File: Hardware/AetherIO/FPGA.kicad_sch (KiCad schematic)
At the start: 3 parts

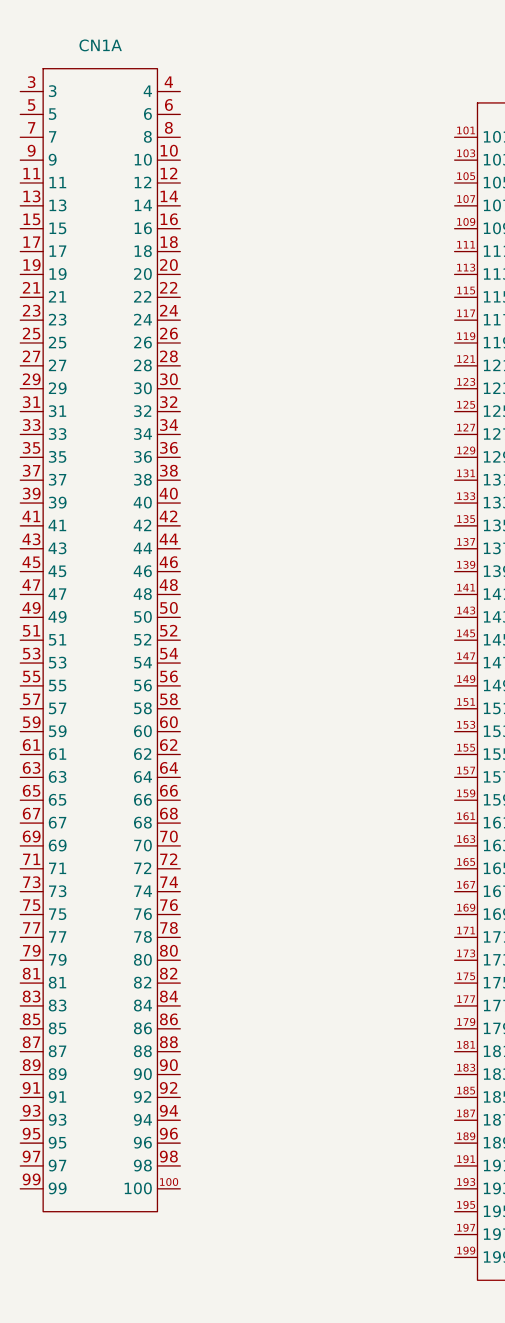
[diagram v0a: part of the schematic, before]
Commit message: add new key and filter design
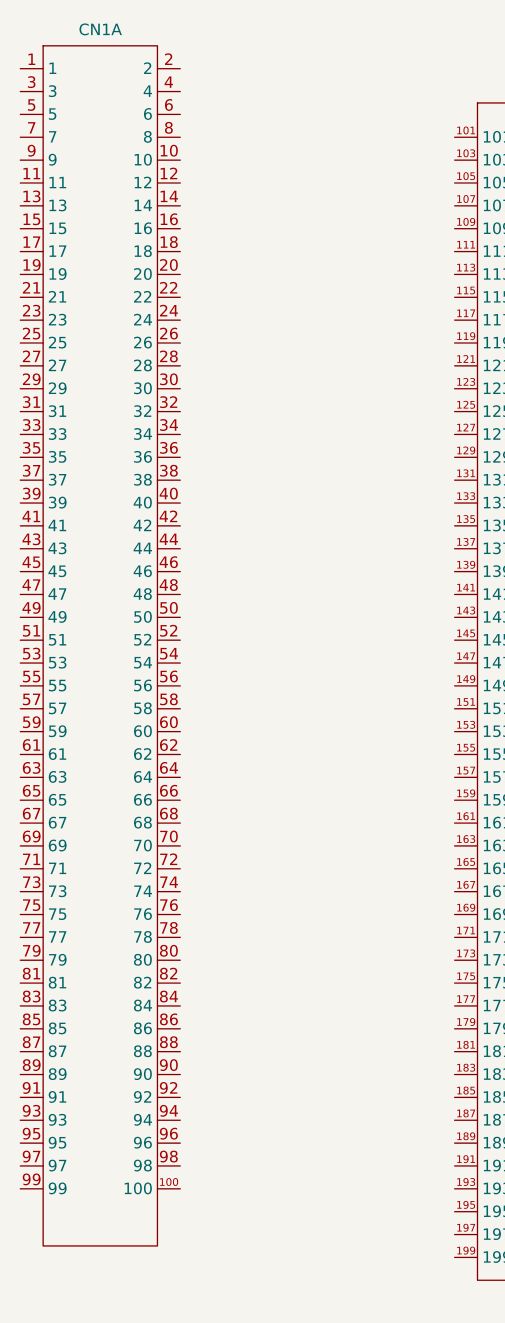
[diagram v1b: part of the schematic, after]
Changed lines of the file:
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@@
 		(on_board yes)
 		(dnp no)
-		(fields_autoplaced yes)
 		(property "Reference" "CN1"
-			(at 36.83 19.05 0)
+			(at 36.83 17.272 0)
 			(effects
 				(font
@@
 		(pin "198"
 		)
+		(pin "2"
+		)
+		(pin "1"
+		)
 		(instances
